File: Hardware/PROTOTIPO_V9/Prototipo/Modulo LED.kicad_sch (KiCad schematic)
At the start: 0 parts

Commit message: Se agrega sch/fp W5500, ILI9341 y fp BluePill
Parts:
- added J4, J8: Conn_01x06, symbol Connector_Generic:Conn_01x06
- added J7, J9: Conn_01x01, symbol Connector_Generic:Conn_01x01
- added U9: CR2013-MI2120, Display:CR2013-MI2120, symbol Driver_Display:CR2013-MI2120
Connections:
- new net: J4.2 (Pin_2), U9.3 (~{CS})
- new net: J7.1 (Pin_1), U9.4 (RESET)
- new net: J4.1 (Pin_1), U9.5 (D/~{C})
- new net: J4.3 (Pin_3), U9.6 (MOSI)
- new net: J4.5 (Pin_5), U9.7 (SCK)
- new net: J4.6 (Pin_6), U9.8 (LED)
- new net: J4.4 (Pin_4), U9.9 (MISO)
- new net +5V_sup: U9.1 (VCC)
- new net CS_Display: J8.2 (Pin_2)
- new net GND_sup: U9.2 (GND)
- new net MISO: J8.4 (Pin_4)
- new net MOSI: J8.3 (Pin_3)
- new net RST_Display: J9.1 (Pin_1)
- no-connect marks 0 -> 7

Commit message: Bus de salida
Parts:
- removed J4, J8: Conn_01x06, symbol Connector_Generic:Conn_01x06
- removed J7, J9: Conn_01x01, symbol Connector_Generic:Conn_01x01
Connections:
- net LCD_CS: now reaches U9.3 (~{CS})
- net LCD_RST: now reaches U9.4 (RESET)
- net LCD_MOSI: now reaches U9.6 (MOSI)
- net LCD_MISO: now reaches U9.9 (MISO)
- net +5V_sup renamed LCD_+5V
- net GND_sup renamed LCD_GND
- no-connect marks 7 -> 8

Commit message: sch ILI9341
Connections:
- net LCD_DC: now reaches U9.5 (D/~{C})
- net LCD_SCK: now reaches U9.7 (SCK)
- net LCD_RST: no longer names the net of U9.4 (RESET)
- no-connect marks 8 -> 6
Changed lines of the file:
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@@
-	)
-	(no_connect
-		(at 128.27 91.44)
 	)
 	(no_connect
@@
 	)
 	(no_connect
-		(at 128.27 101.6)
-	)
-	(no_connect
 		(at 87.63 88.9)
 	)
@@
 		(pts
 			(xy 107.95 118.11) (xy 134.62 118.11)
+		)
+		(stroke
+			(width 0)
+			(type default)
+		)
+	)
+	(wire
+		(pts
+			(xy 128.27 101.6) (xy 140.97 101.6)
+		)
+		(stroke
+			(width 0)
+			(type default)
+		)
+	)
+	(wire
+		(pts
+			(xy 128.27 91.44) (xy 140.97 91.44)
 		)
 		(stroke
@@
 		)
 	)
-	(hierarchical_label "LCD_RST"
-		(shape input)
-		(at 140.97 106.68 0)
-		(effects
-			(font
-				(size 1.27 1.27)
-			)
-			(justify left)
-		)
-	)
 	(hierarchical_label "LCD_GND"
 		(shape output)
@@
 		(effects
 			(font
+				(size 1.27 1.27)
+			)
+			(justify left)
+		)
+	)
+	(hierarchical_label "LCD_DC"
+		(shape input)
+		(at 140.97 91.44 0)
+		(effects
+			(font
+				(size 1.27 1.27)
+			)
+			(justify left)
+		)
+	)
+	(hierarchical_label "LCD_SCK"
+		(shape input)
+		(at 140.97 101.6 0)
+		(effects
+			(font

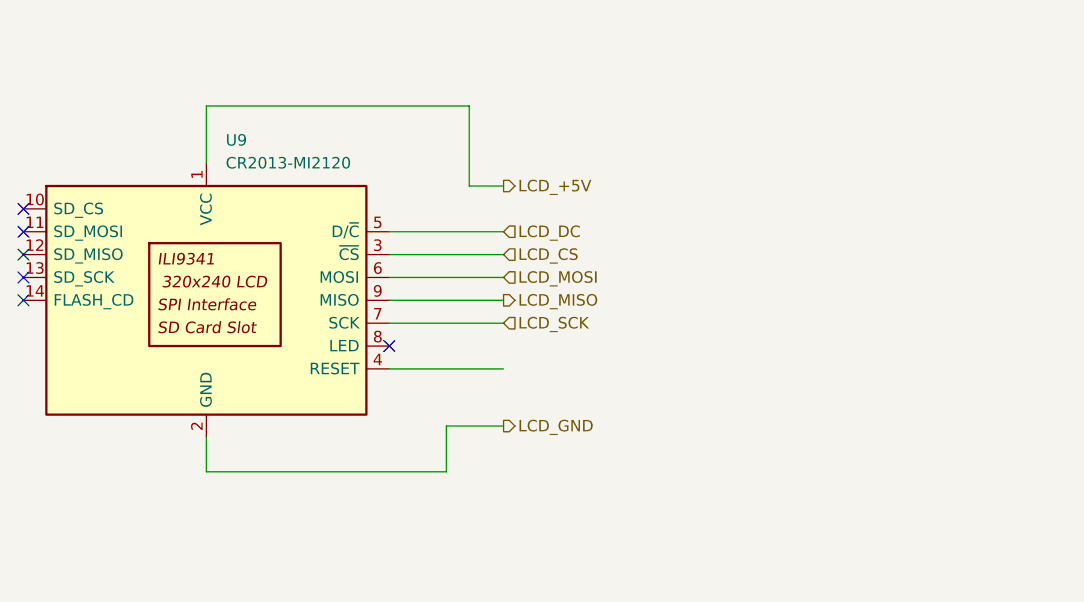
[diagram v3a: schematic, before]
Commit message: sch ILI9341 y sch ADS1115
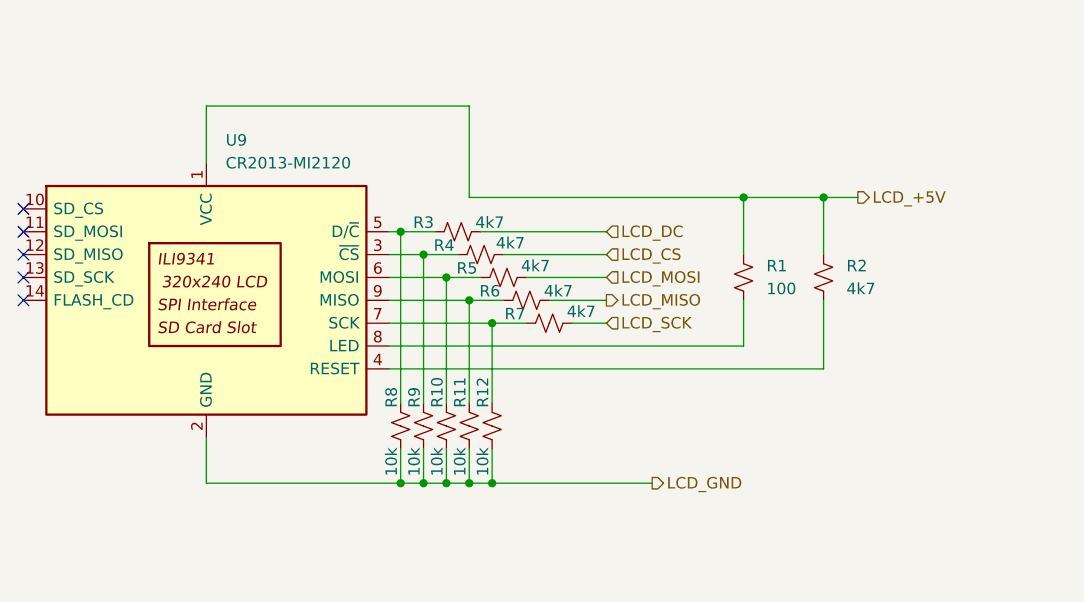
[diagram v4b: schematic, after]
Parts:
- added R1: 100, symbol Device:R_Small_US
- added R10, R11, R12, R8, R9: 10k, symbol Device:R_Small_US
- added R2, R3, R4, R5, R6, R7: 4k7, symbol Device:R_Small_US
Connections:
- net LCD_+5V: now also R1.1, R2.1
- net LCD_CS: now also R4.2; no longer U9.3 (~{CS})
- net LCD_DC: now also R3.2; no longer U9.5 (D/~{C})
- net LCD_GND: now also R10.2, R11.2, R12.2, R8.2, R9.2
- net LCD_MISO: now also R6.2; no longer U9.9 (MISO)
- net LCD_MOSI: now also R5.2; no longer U9.6 (MOSI)
- net LCD_SCK: now also R7.2; no longer U9.7 (SCK)
- net at U9.4 (RESET): now also R2.2
- net at U9.8 (LED): now also R1.2
- new net: R12.1, R7.1, U9.7 (SCK)
- new net: R10.1, R5.1, U9.6 (MOSI)
- new net: R4.1, R9.1, U9.3 (~{CS})
- new net: R3.1, R8.1, U9.5 (D/~{C})
- new net: R11.1, R6.1, U9.9 (MISO)
- no-connect marks 6 -> 5

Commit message: Asignación de huellas
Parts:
- R1, R10, R11, R12, R2, R3, R4, R5, R6, R7, R8, R9: footprint (none) -> Resistor_THT:R_Axial_DIN0207_L6.3mm_D2.5mm_P10.16mm_Horizontal
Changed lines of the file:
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@@
 			)
 		)
-		(property "Footprint" ""
+		(property "Footprint" "Resistor_THT:R_Axial_DIN0207_L6.3mm_D2.5mm_P10.16mm_Horizontal"
 			(at 146.05 101.6 0)
 			(effects
@@
 			)
 		)
-		(property "Footprint" ""
+		(property "Footprint" "Resistor_THT:R_Axial_DIN0207_L6.3mm_D2.5mm_P10.16mm_Horizontal"
 			(at 167.64 96.52 0)
 			(effects
@@
 			)
 		)
-		(property "Footprint" ""
+		(property "Footprint" "Resistor_THT:R_Axial_DIN0207_L6.3mm_D2.5mm_P10.16mm_Horizontal"
 			(at 134.62 113.03 0)
 			(effects
@@
 			)
 		)
-		(property "Footprint" ""
+		(property "Footprint" "Resistor_THT:R_Axial_DIN0207_L6.3mm_D2.5mm_P10.16mm_Horizontal"
 			(at 176.53 96.52 0)
 			(effects
@@
 			)
 		)
-		(property "Footprint" ""
+		(property "Footprint" "Resistor_THT:R_Axial_DIN0207_L6.3mm_D2.5mm_P10.16mm_Horizontal"
 			(at 140.97 96.52 0)
 			(effects
@@
 			)
 		)
-		(property "Footprint" ""
+		(property "Footprint" "Resistor_THT:R_Axial_DIN0207_L6.3mm_D2.5mm_P10.16mm_Horizontal"
 			(at 132.08 113.03 0)
 			(effects
@@
 			)
 		)
-		(property "Footprint" ""
+		(property "Footprint" "Resistor_THT:R_Axial_DIN0207_L6.3mm_D2.5mm_P10.16mm_Horizontal"
 			(at 138.43 93.98 0)
 			(effects
@@
 			)
 		)
-		(property "Footprint" ""
+		(property "Footprint" "Resistor_THT:R_Axial_DIN0207_L6.3mm_D2.5mm_P10.16mm_Horizontal"
 			(at 129.54 113.03 0)
 			(effects
@@
 			)
 		)
-		(property "Footprint" ""
+		(property "Footprint" "Resistor_THT:R_Axial_DIN0207_L6.3mm_D2.5mm_P10.16mm_Horizontal"
 			(at 137.16 113.03 0)
 			(effects
@@
 			)
 		)
-		(property "Footprint" ""
+		(property "Footprint" "Resistor_THT:R_Axial_DIN0207_L6.3mm_D2.5mm_P10.16mm_Horizontal"
 			(at 143.51 99.06 0)
 			(effects
@@
 			)
 		)
-		(property "Footprint" ""
+		(property "Footprint" "Resistor_THT:R_Axial_DIN0207_L6.3mm_D2.5mm_P10.16mm_Horizontal"
 			(at 135.89 91.44 0)
 			(effects
@@
 			)
 		)
-		(property "Footprint" ""
+		(property "Footprint" "Resistor_THT:R_Axial_DIN0207_L6.3mm_D2.5mm_P10.16mm_Horizontal"
 			(at 139.7 113.03 0)
 			(effects

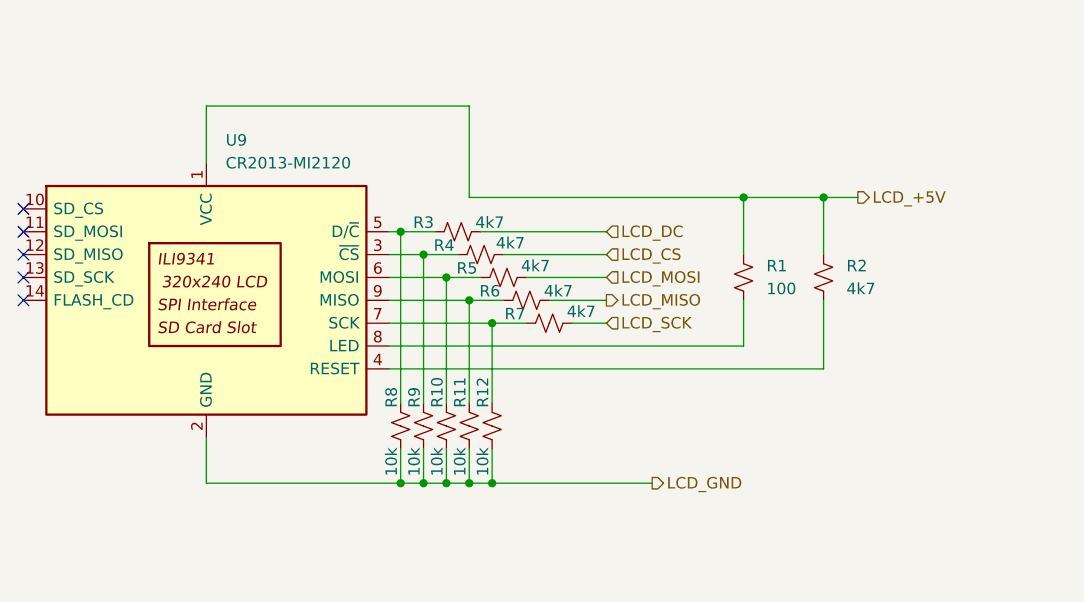
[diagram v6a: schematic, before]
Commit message: Migrar a BlackPill
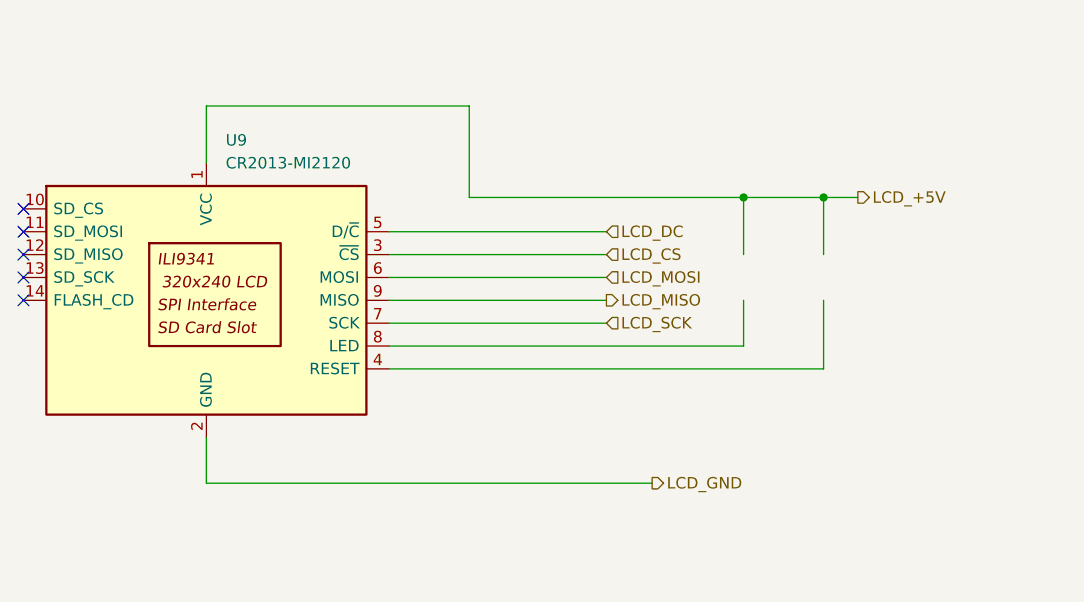
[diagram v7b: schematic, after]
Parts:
- removed R1: 100, Resistor_THT:R_Axial_DIN0207_L6.3mm_D2.5mm_P10.16mm_Horizontal, symbol Device:R_Small_US
- removed R10, R11, R12, R8, R9: 10k, Resistor_THT:R_Axial_DIN0207_L6.3mm_D2.5mm_P10.16mm_Horizontal, symbol Device:R_Small_US
- removed R2, R3, R4, R5, R6, R7: 4k7, Resistor_THT:R_Axial_DIN0207_L6.3mm_D2.5mm_P10.16mm_Horizontal, symbol Device:R_Small_US
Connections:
- net LCD_CS: now also U9.3 (~{CS})
- net LCD_DC: now also U9.5 (D/~{C})
- net LCD_MISO: now also U9.9 (MISO)
- net LCD_MOSI: now also U9.6 (MOSI)
- net LCD_SCK: now also U9.7 (SCK)
